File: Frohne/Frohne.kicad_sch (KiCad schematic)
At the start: 6 parts

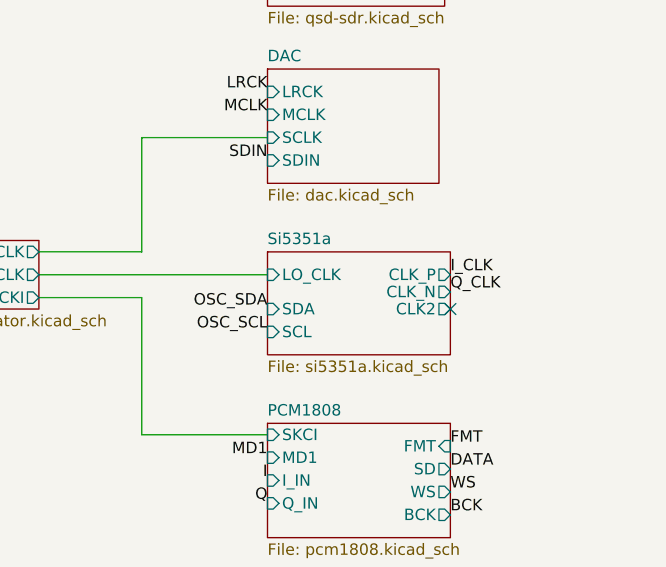
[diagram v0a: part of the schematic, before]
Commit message: Added R37 asd R38
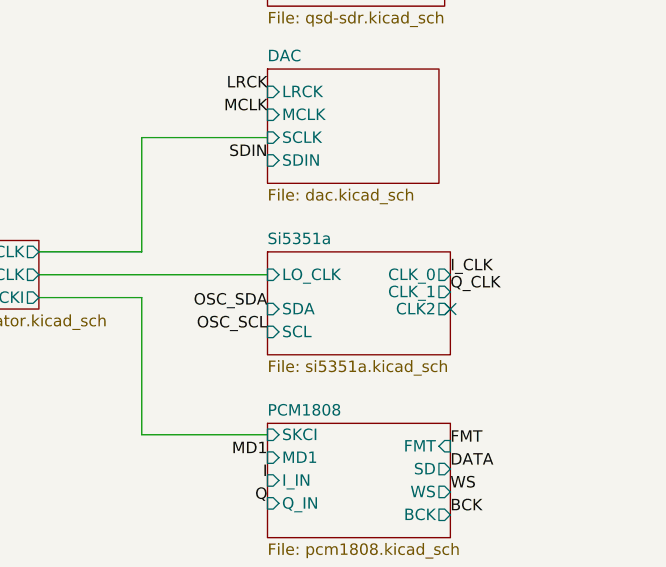
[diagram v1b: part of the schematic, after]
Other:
- sheet Si5351a ports: added CLK_0, CLK_1; removed CLK_N, CLK_P
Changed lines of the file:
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@@
 			)
 		)
-		(pin "CLK_P" output
+		(pin "CLK_0" output
 			(at 82.55 158.75 0)
 			(effects
@@
 			)
 		)
-		(pin "CLK_N" output
+		(pin "CLK_1" output
 			(at 82.55 160.655 0)
 			(effects
